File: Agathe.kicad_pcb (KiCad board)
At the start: 2 copper layers, 338.8 x 129.1 mm, 194 parts, among them J1 Conn_01x04_Female, J2 Conn_01x04_Female, J3 AVR-ISP-6, SW1 SW_Push, U1 ATmega32U4-AU, U2 PRTR5V0U2X, Y1 16MHz

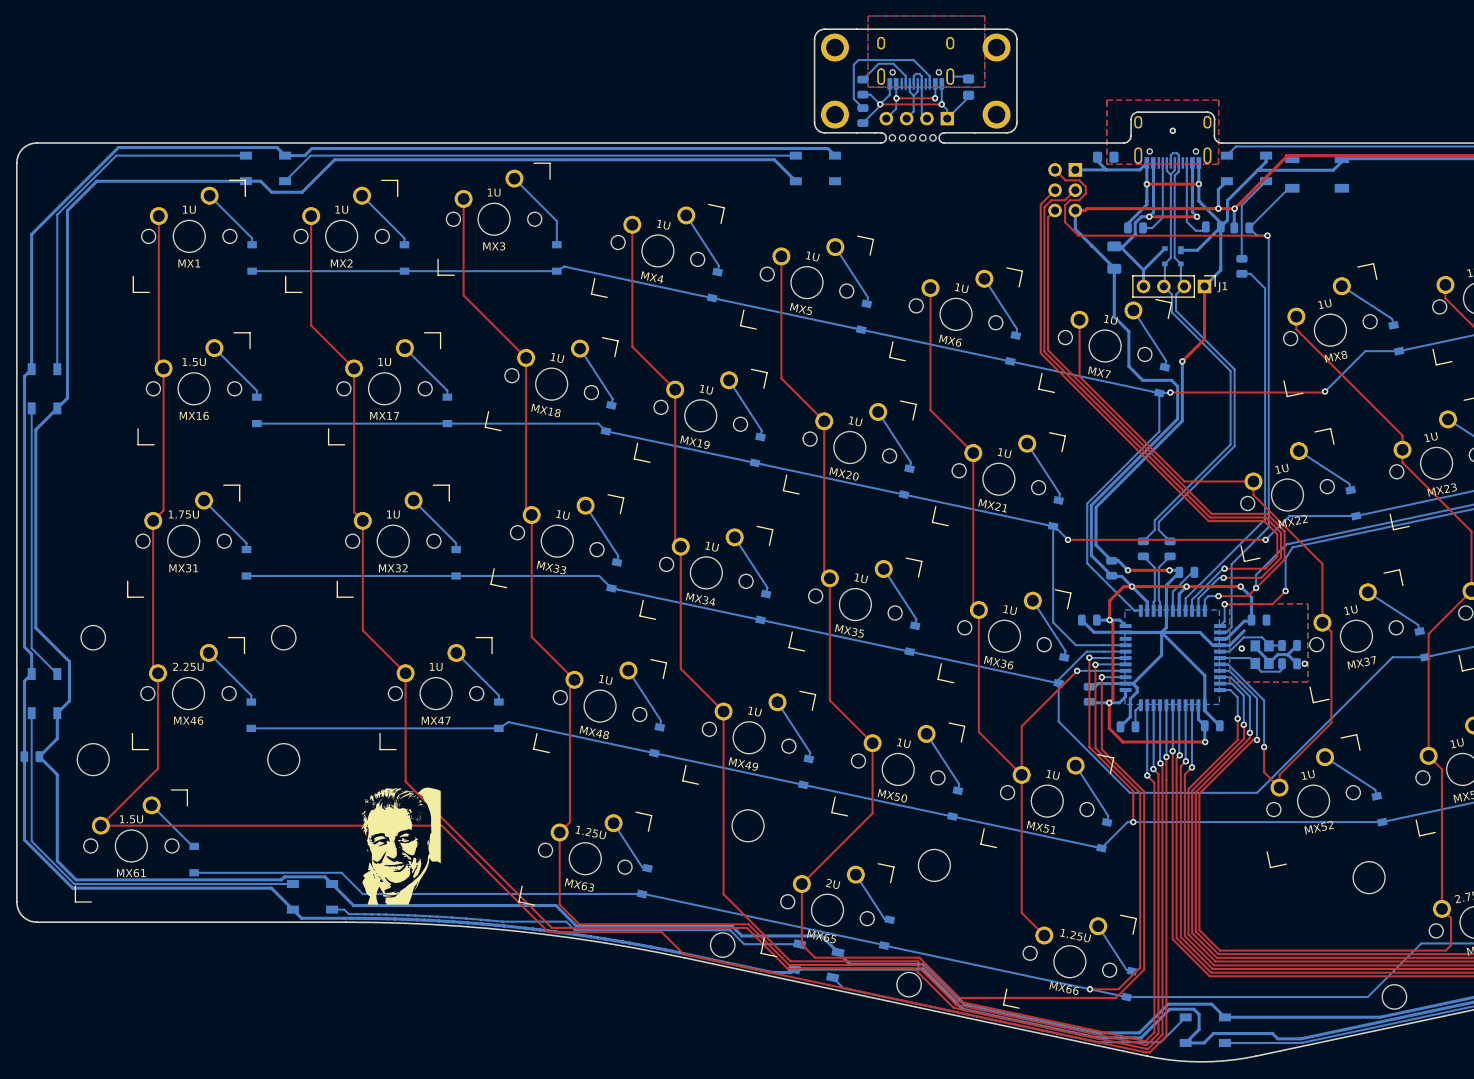
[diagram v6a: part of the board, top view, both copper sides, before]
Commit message: move the daughterboard at the bottom and change the mcu
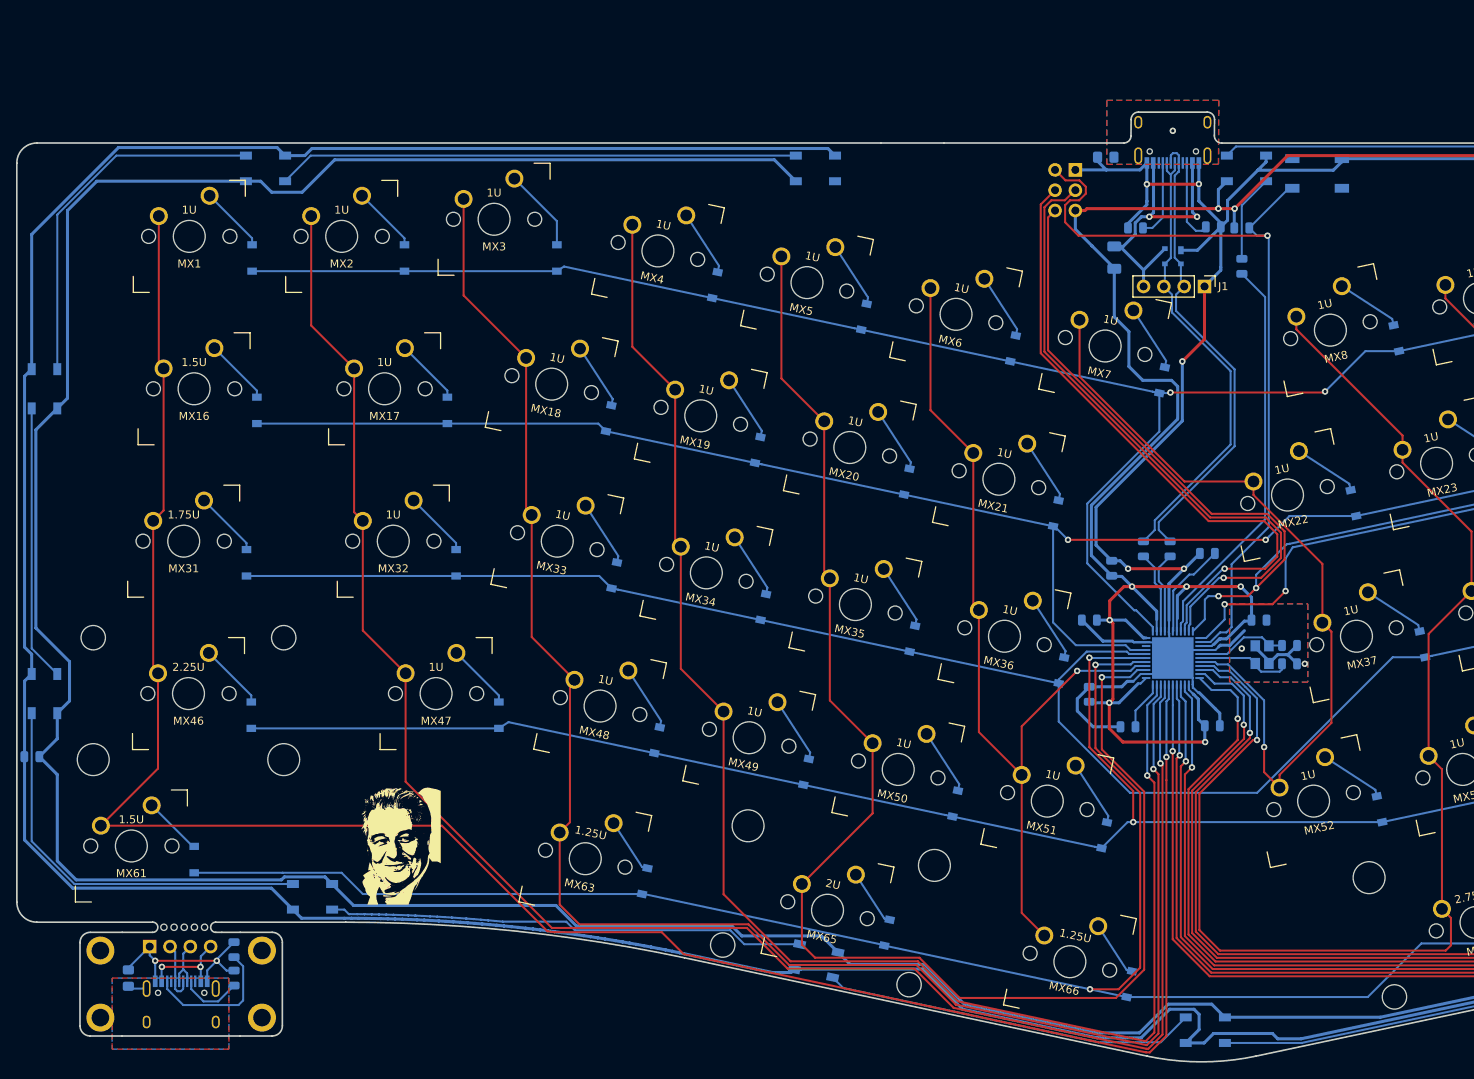
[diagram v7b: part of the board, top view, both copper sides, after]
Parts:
- removed the REF** at (159.1, 103.6)
- removed the REF** at (159.1, 112.0)
- removed the REF** at (138.9, 112.0)
- added REF**: Generic-Mounthole, random-keyboard-parts:Generic-Mounthole, F.Cu at (47.0, 224.9)
- added REF**: Generic-Mounthole, random-keyboard-parts:Generic-Mounthole, F.Cu at (47.0, 216.5)
- added REF**: Generic-Mounthole, random-keyboard-parts:Generic-Mounthole, F.Cu at (67.2, 216.5)
- R7: value 350 -> 330
- U1: footprint Keebio-Parts:ATMEGA32U4-AU -> Package_DFN_QFN:QFN-44-1EP_7x7mm_P0.5mm_EP5.2x5.2mm
- moved FB2 153.1 mm to (50.5, 220.0), turned to 270 degrees
- moved USB2 151.3 mm to (57.1, 224.4), turned to 180 degrees
- moved J2 143.7 mm to (53.2, 216.0), turned to 270 degrees
- moved REF** 140.8 mm to (67.2, 224.9), turned to 180 degrees
- moved R9 136.3 mm to (63.8, 220.0), turned to 270 degrees
- moved REF** 134.3 mm to (57.5, 213.9)
- moved R8 130.6 mm to (63.8, 216.4), turned to 270 degrees
- moved C1 3.48 mm to (185.4, 166.9)
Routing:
- net +5V: track 993.4 -> 1011.2 mm
- net GND: track 1026.3 -> 1034.4 mm
- net Net-(C1-Pad1): track 6.08 -> 12.2 mm
- net MISO: track 292.9 -> 296.1 mm
- net COL10: track 224.1 -> 227.3 mm
- net Net-(R1-Pad2): track 2.97 -> 6.16 mm
- net RST: track 99.9 -> 102.9 mm
- net MOSI: track 78.9 -> 81.9 mm
- net COL9: track 197.6 -> 200.7 mm
- net COL3: track 190.1 -> 193.1 mm
- net ROTB: track 236.1 -> 239.1 mm
- net COL2: track 217.2 -> 220.1 mm
- net SCK: track 77.1 -> 80.1 mm
- net COL4: track 183.1 -> 186.1 mm
- net COL8: track 177.9 -> 180.9 mm
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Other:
- board size 338.8 x 129.1 mm -> 338.8 x 118.7 mm

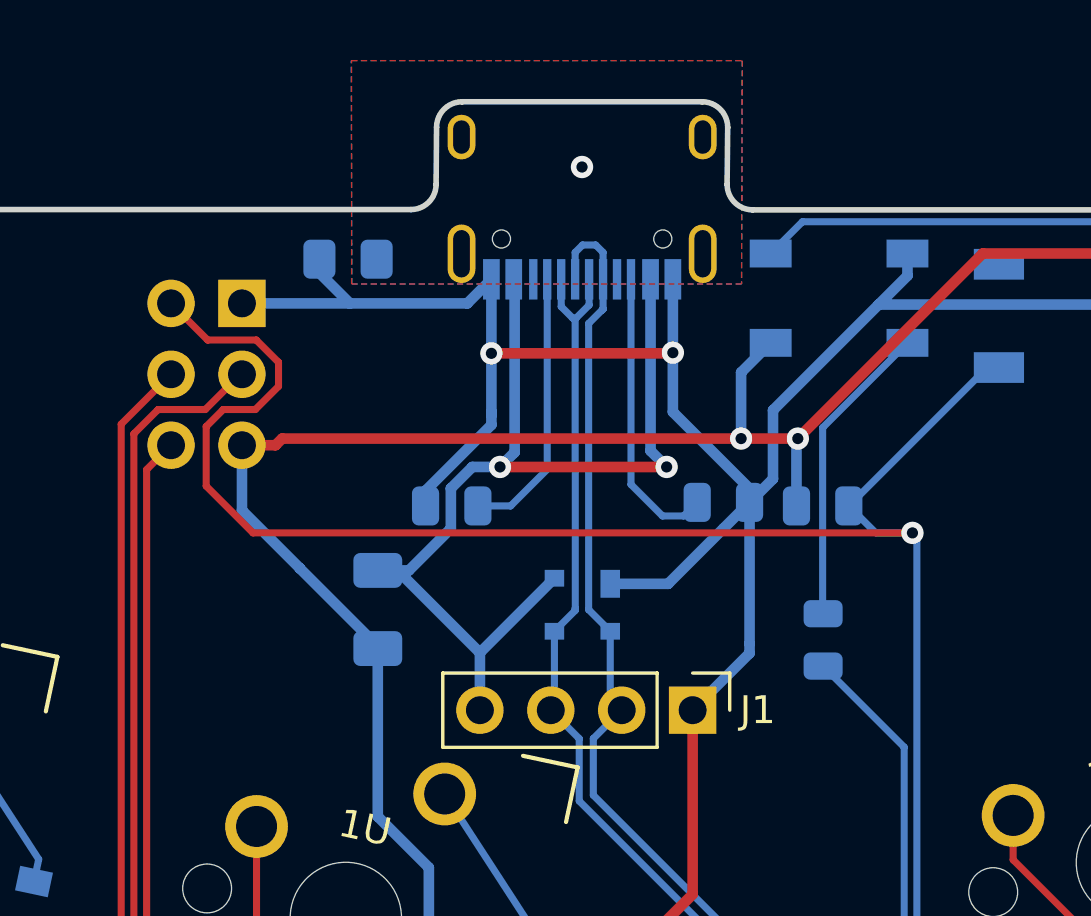
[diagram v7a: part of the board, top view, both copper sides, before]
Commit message: top mount usb-port
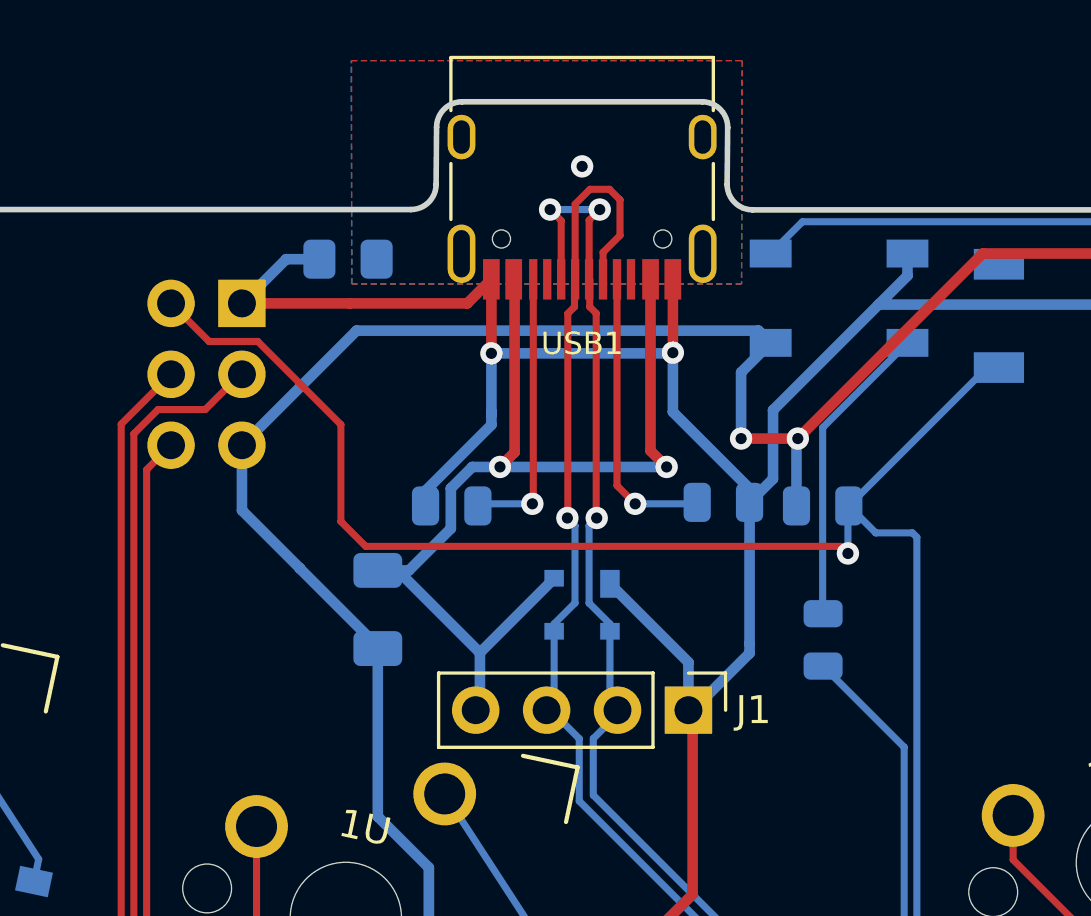
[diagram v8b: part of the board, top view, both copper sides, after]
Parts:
- USB1: moved to F.Cu
- moved J1 0.15 mm to (184.9, 133.5)
- turned USB1 to 180 degrees
- renumbered R6 to R5, R5 to R6
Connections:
- R5 pad 2: Net-(R6-Pad2) -> Net-(R5-Pad2)
- R6 pad 2: Net-(R5-Pad2) -> Net-(R6-Pad2)
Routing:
- net DN: track 57.5 -> 63.9 mm, vias 0 -> 1
- net RST: track 102.9 -> 97.7 mm
- net DP: track 59.2 -> 63.6 mm, vias 0 -> 3
- net +5V: track 1011.2 -> 1014.0 mm
- net GND: track 1034.4 -> 1035.8 mm
- net Net-(R5-Pad2): track 9.79 -> 10.6 mm, vias 0 -> 1
- net Net-(R6-Pad2): track 10.3 -> 10.0 mm, vias 0 -> 1
